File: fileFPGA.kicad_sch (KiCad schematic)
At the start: 11 parts, among them J2 UART, J6 JTAG, U3 LFE5U-25F-6BG256C, U6 W25Q128JVP

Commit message: Update Mouser prices
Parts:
- C25: Pricing (EUR) 0,11 -> 0,09
- C26: Pricing (EUR) 0,09 -> 0,02
- J2: Pricing (EUR) 0,24 -> 0,32
- J6: Pricing (EUR) 2,37 -> 3,02
- OSC1: Pricing (EUR) 1,13 -> 1,23
- R27, R30: Pricing (EUR) 0,11 -> 0,10
- U3: Pricing (EUR) 7,87 -> 14,25
- U6: Pricing (EUR) 1,52 -> 1,94
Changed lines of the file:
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@@
       (effects (font (size 1.27 1.27)) hide)
     )
-    (property "Pricing (EUR)" "2,37" (id 7) (at 218.44 27.94 0)
+    (property "Pricing (EUR)" "3,02" (id 7) (at 218.44 27.94 0)
       (effects (font (size 1.27 1.27)) hide)
     )
@@
       (effects (font (size 1.27 1.27)) hide)
     )
-    (property "Pricing (EUR)" "0,11" (id 7) (at 187.96 30.48 0)
+    (property "Pricing (EUR)" "0,10" (id 7) (at 187.96 30.48 0)
       (effects (font (size 1.27 1.27)) hide)
     )
@@
       (effects (font (size 1.27 1.27)) hide)
     )
-    (property "Pricing (EUR)" "1,52" (id 8) (at 57.15 181.61 0)
+    (property "Pricing (EUR)" "1,94" (id 8) (at 57.15 181.61 0)
       (effects (font (size 1.27 1.27)) hide)
     )
@@
       (effects (font (size 1.27 1.27)) hide)
     )
-    (property "Pricing (EUR)" "1,13" (id 7) (at 142.24 180.34 0)
+    (property "Pricing (EUR)" "1,23" (id 7) (at 142.24 180.34 0)
       (effects (font (size 1.27 1.27)) hide)
     )
@@
       (effects (font (size 1.27 1.27)) hide)
     )
-    (property "Pricing (EUR)" "0,11" (id 7) (at 179.07 66.04 0)
+    (property "Pricing (EUR)" "0,09" (id 7) (at 179.07 66.04 0)
       (effects (font (size 1.27 1.27)) hide)
     )
@@
       (effects (font (size 1.27 1.27)) hide)
     )
-    (property "Pricing (EUR)" "0,09" (id 7) (at 184.15 66.04 0)
+    (property "Pricing (EUR)" "0,02" (id 7) (at 184.15 66.04 0)
       (effects (font (size 1.27 1.27)) hide)
     )
@@
       (effects (font (size 1.27 1.27)) hide)
     )
-    (property "Pricing (EUR)" "0,11" (id 7) (at 40.64 168.91 0)
+    (property "Pricing (EUR)" "0,10" (id 7) (at 40.64 168.91 0)
       (effects (font (size 1.27 1.27)) hide)
     )
@@
       (effects (font (size 1.27 1.27)) hide)
     )
-    (property "Pricing (EUR)" "7,87" (id 7) (at 36.83 34.29 0)
+    (property "Pricing (EUR)" "14,25" (id 7) (at 36.83 34.29 0)
       (effects (font (size 1.27 1.27)) hide)
     )
@@
       (effects (font (size 1.27 1.27)) hide)
     )
-    (property "Pricing (EUR)" "7,87" (id 7) (at 121.92 31.75 0)
+    (property "Pricing (EUR)" "14,25" (id 7) (at 121.92 31.75 0)
       (effects (font (size 1.27 1.27)) hide)
     )
@@
       (effects (font (size 1.27 1.27)) hide)
     )
-    (property "Pricing (EUR)" "7,87" (id 7) (at 185.42 77.47 0)
+    (property "Pricing (EUR)" "14,25" (id 7) (at 185.42 77.47 0)
       (effects (font (size 1.27 1.27)) hide)
     )
@@
       (effects (font (size 1.27 1.27)) hide)
     )
-    (property "Pricing (EUR)" "7,87" (id 7) (at 248.92 34.29 0)
+    (property "Pricing (EUR)" "14,25" (id 7) (at 248.92 34.29 0)
       (effects (font (size 1.27 1.27)) hide)
     )
@@
       (effects (font (size 1.27 1.27)) hide)
     )
-    (property "Pricing (EUR)" "0,24" (id 7) (at 217.17 52.07 0)
-      (effects (font (size 1.27 1.27)) hide)
-    )
+    (property "Pricing (EUR)" "0,32" (id 7) (at 217.17 52.07 0)
+      (effects (font (size 1.27 1.27)) hide)
+    )

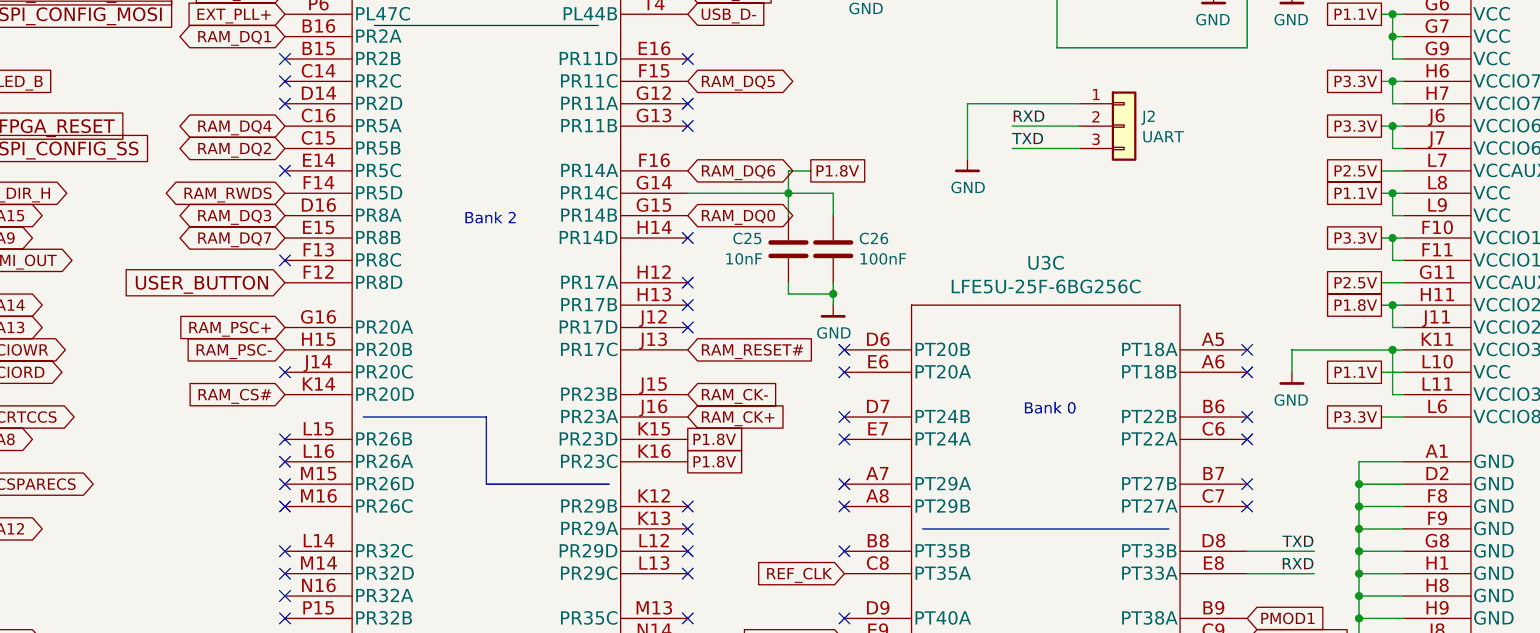
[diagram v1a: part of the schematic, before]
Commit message: Replace HyperRAM with 3V Winbond part
Also remove PSC/PSC# as they are not used on 3V parts.
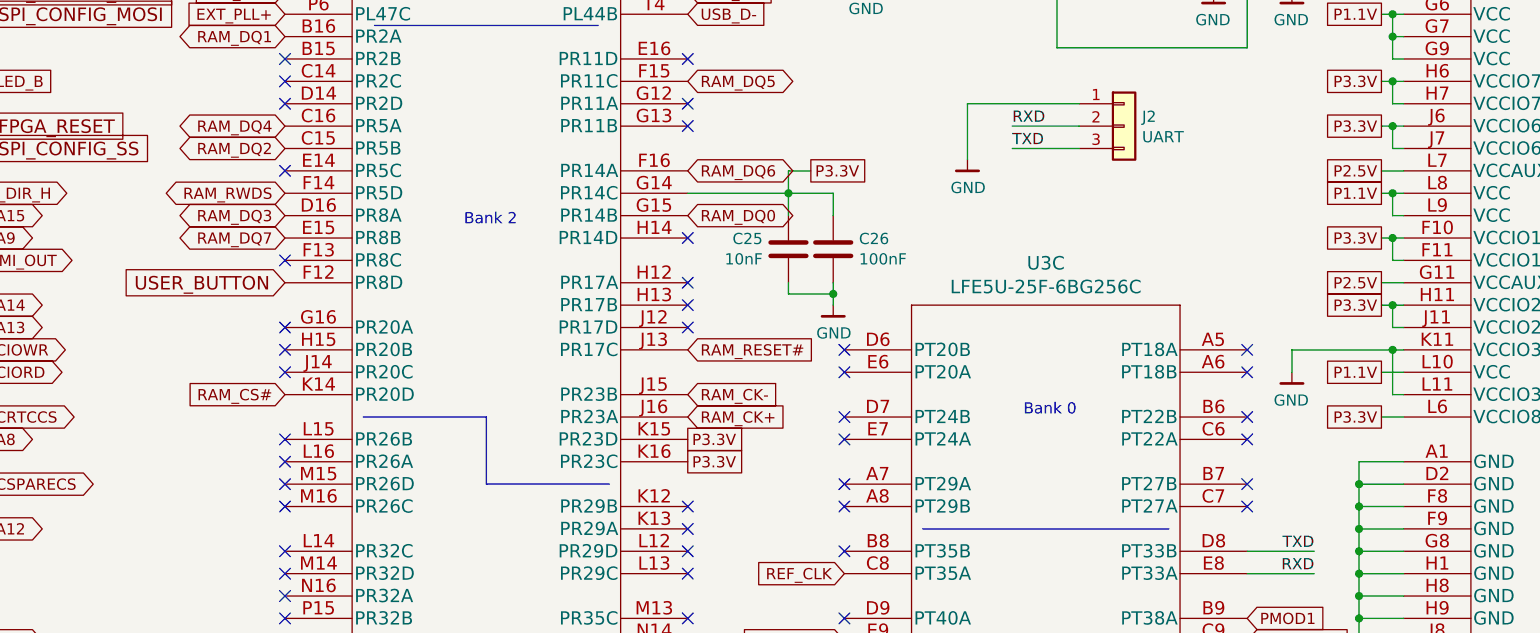
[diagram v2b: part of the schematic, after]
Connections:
- net P1.8V is gone; now on net P3.3V: C25.1, C26.1, U3.G14 (PR14C), U3.H11 (VCCIO2), U3.J11 (VCCIO2), U3.K15 (PR23D), U3.K16 (PR23C)
- net RAM_PSC+: no longer names the net of U3.G16 (PR20A)
- net RAM_PSC-: no longer names the net of U3.H15 (PR20B)
- no-connect marks 101 -> 103
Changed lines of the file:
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@@
   )
   (no_connect (at 121.92 105.41))
+  (no_connect (at 121.92 74.93))
+  (no_connect (at 121.92 77.47))
   (no_connect (at 231.14 85.09))
   (no_connect (at 87.63 135.89))
@@
     )
   )
+  (global_label "P3.3V" (shape passive) (at 167.64 87.63 0) (fields_autoplaced)
+    (effects (font (size 1.27 1.27)) (justify left))
+    (property "Intersheet References" "${INTERSHEET_REFS}" (id 0) (at 414.02 152.4 0)
+      (effects (font (size 1.27 1.27)) hide)
+    )
+  )
   (global_label "REF_CLK" (shape input) (at 152.4 181.61 0) (fields_autoplaced)
     (effects (font (size 1.27 1.27)) (justify left))
@@
     )
   )
-  (global_label "P1.8V" (shape passive) (at 181.61 57.15 0) (fields_autoplaced)
-    (effects (font (size 1.27 1.27)) (justify left))
-    (property "Intersheet References" "${INTERSHEET_REFS}" (id 0) (at 0 0 0)
-      (effects (font (size 1.27 1.27)) hide)
-    )
-  )
   (global_label "A0" (shape bidirectional) (at 121.92 31.75 180) (fields_autoplaced)
     (effects (font (size 1.27 1.27)) (justify right))
@@
     )
   )
+  (global_label "P3.3V" (shape passive) (at 181.61 57.15 0) (fields_autoplaced)
+    (effects (font (size 1.27 1.27)) (justify left))
+    (property "Intersheet References" "${INTERSHEET_REFS}" (id 0) (at 427.99 121.92 0)
+      (effects (font (size 1.27 1.27)) hide)
+    )
+  )
   (global_label "RAM_DQ7" (shape bidirectional) (at 121.92 64.77 180) (fields_autoplaced)
     (effects (font (size 1.27 1.27)) (justify right))
@@
     )
   )
-  (global_label "P1.8V" (shape passive) (at 246.38 72.39 180) (fields_autoplaced)
-    (effects (font (size 1.27 1.27)) (justify right))
-    (property "Intersheet References" "${INTERSHEET_REFS}" (id 0) (at 0 0 0)
-      (effects (font (size 1.27 1.27)) hide)
-    )
-  )
-  (global_label "RAM_PSC+" (shape input) (at 121.92 74.93 180) (fields_autoplaced)
-    (effects (font (size 1.27 1.27)) (justify right))
-    (property "Intersheet References" "${INTERSHEET_REFS}" (id 0) (at 0 0 0)
-      (effects (font (size 1.27 1.27)) hide)
-    )
-  )
   (global_label "P2.5V" (shape passive) (at 246.38 69.85 180) (fields_autoplaced)
     (effects (font (size 1.27 1.27)) (justify right))
@@
   (global_label "A6" (shape bidirectional) (at 36.83 130.81 180) (fields_autoplaced)
     (effects (font (size 1.27 1.27)) (justify right))
-    (property "Intersheet References" "${INTERSHEET_REFS}" (id 0) (at 0 0 0)
-      (effects (font (size 1.27 1.27)) hide)
-    )
-  )
-  (global_label "P1.8V" (shape passive) (at 167.64 90.17 0) (fields_autoplaced)
-    (effects (font (size 1.27 1.27)) (justify left))
     (property "Intersheet References" "${INTERSHEET_REFS}" (id 0) (at 0 0 0)
       (effects (font (size 1.27 1.27)) hide)
@@
     )
   )
-  (global_label "RAM_PSC-" (shape input) (at 121.92 77.47 180) (fields_autoplaced)
-    (effects (font (size 1.27 1.27)) (justify right))
-    (property "Intersheet References" "${INTERSHEET_REFS}" (id 0) (at 0 0 0)
-      (effects (font (size 1.27 1.27)) hide)
-    )
-  )
   (global_label "A10" (shape bidirectional) (at 87.63 110.49 0) (fields_autoplaced)
     (effects (font (size 1.27 1.27)) (justify left))
@@
     )
   )
+  (global_label "P3.3V" (shape passive) (at 246.38 72.39 180) (fields_autoplaced)
+    (effects (font (size 1.27 1.27)) (justify right))
+    (property "Intersheet References" "${INTERSHEET_REFS}" (id 0) (at 0 7.62 0)
+      (effects (font (size 1.27 1.27)) hide)
+    )
+  )
   (global_label "A_~{EN}_L" (shape output) (at 36.83 115.57 180) (fields_autoplaced)
     (effects (font (size 1.27 1.27)) (justify right))
@@
   )
   (global_label "A11" (shape bidirectional) (at 87.63 113.03 0) (fields_autoplaced)
-    (effects (font (size 1.27 1.27)) (justify left))
-    (property "Intersheet References" "${INTERSHEET_REFS}" (id 0) (at 0 0 0)
-      (effects (font (size 1.27 1.27)) hide)
-    )
-  )
-  (global_label "P1.8V" (shape passive) (at 167.64 87.63 0) (fields_autoplaced)
     (effects (font (size 1.27 1.27)) (justify left))
     (property "Intersheet References" "${INTERSHEET_REFS}" (id 0) (at 0 0 0)
@@
       (effects (font (size 1.27 1.27)) hide)
     )
+  )
+  (global_label "P3.3V" (shape passive) (at 167.64 90.17 0) (fields_autoplaced)
+    (effects (font (size 1.27 1.27)) (justify left))
+    (property "Intersheet References" "${INTERSHEET_REFS}" (id 0) (at 414.02 154.94 0)
+      (effects (font (size 1.27 1.27)) hide)
+    )

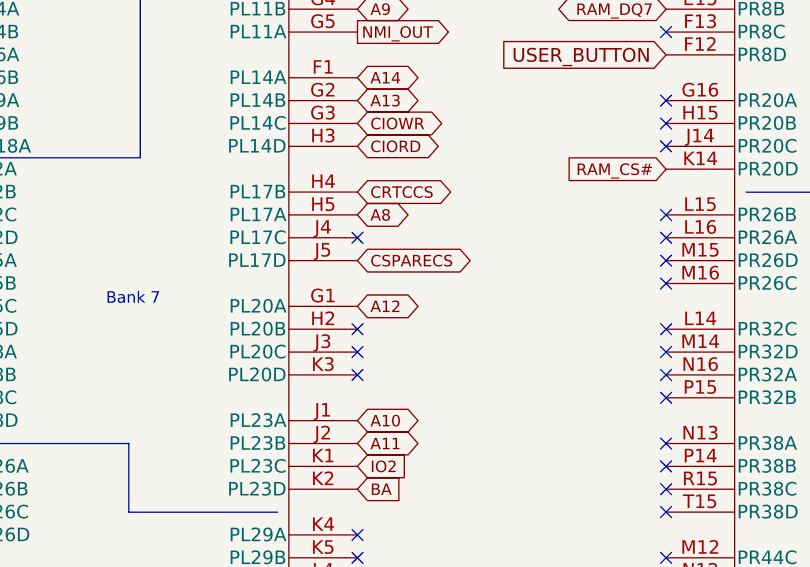
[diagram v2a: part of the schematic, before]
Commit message: Add NMI and IRQ inputs
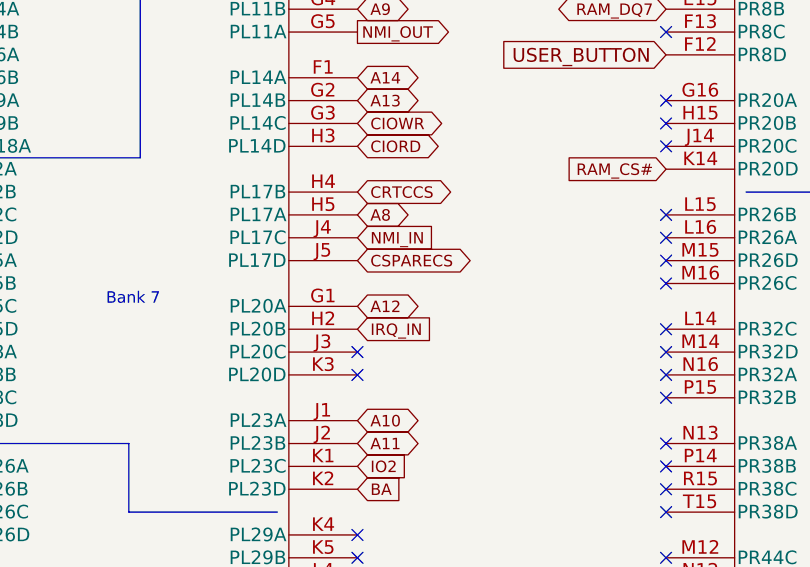
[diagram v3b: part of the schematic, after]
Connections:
- net IRQ_IN: now reaches U3.H2 (PL20B)
- net NMI_IN: now reaches U3.J4 (PL17C)
- no-connect marks 103 -> 101
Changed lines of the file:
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@@
   (no_connect (at 167.64 138.43))
   (no_connect (at 231.14 77.47))
-  (no_connect (at 87.63 90.17))
   (no_connect (at 167.64 95.25))
   (no_connect (at 167.64 156.21))
   (no_connect (at 36.83 72.39))
   (no_connect (at 121.92 49.53))
-  (no_connect (at 87.63 100.33))
   (no_connect (at 121.92 80.01))
   (no_connect (at 167.64 148.59))
@@
     )
   )
+  (global_label "IRQ_IN" (shape input) (at 87.63 100.33 0) (fields_autoplaced)
+    (effects (font (size 1.27 1.27)) (justify left))
+    (property "Intersheet References" "${INTERSHEET_REFS}" (id 0) (at 96.0623 100.2506 0)
+      (effects (font (size 1.27 1.27)) (justify left) hide)
+    )
+  )
   (global_label "A8" (shape bidirectional) (at 87.63 87.63 0) (fields_autoplaced)
     (effects (font (size 1.27 1.27)) (justify left))
@@
     )
   )
+  (global_label "NMI_IN" (shape input) (at 87.63 90.17 0) (fields_autoplaced)
+    (effects (font (size 1.27 1.27)) (justify left))
+    (property "Intersheet References" "${INTERSHEET_REFS}" (id 0) (at 96.2437 90.0906 0)
+      (effects (font (size 1.27 1.27)) (justify left) hide)
+    )
+  )

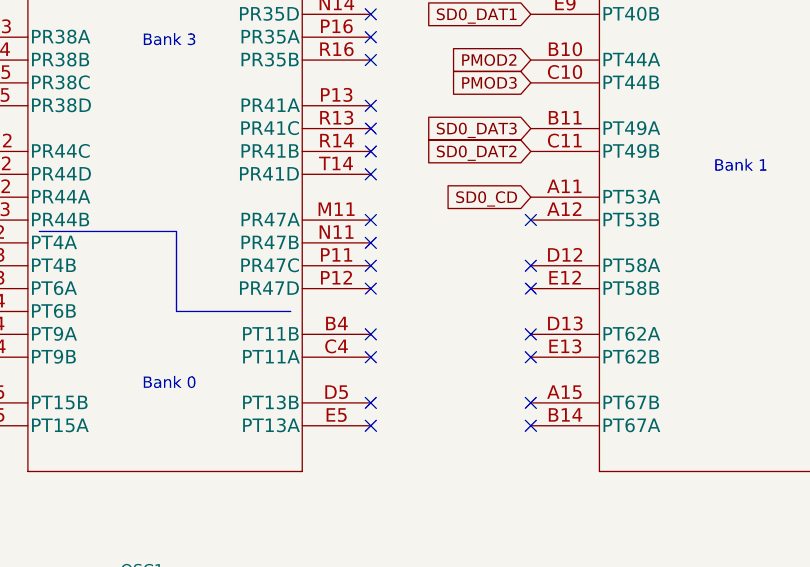
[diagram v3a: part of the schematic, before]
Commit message: Redo routing to memories
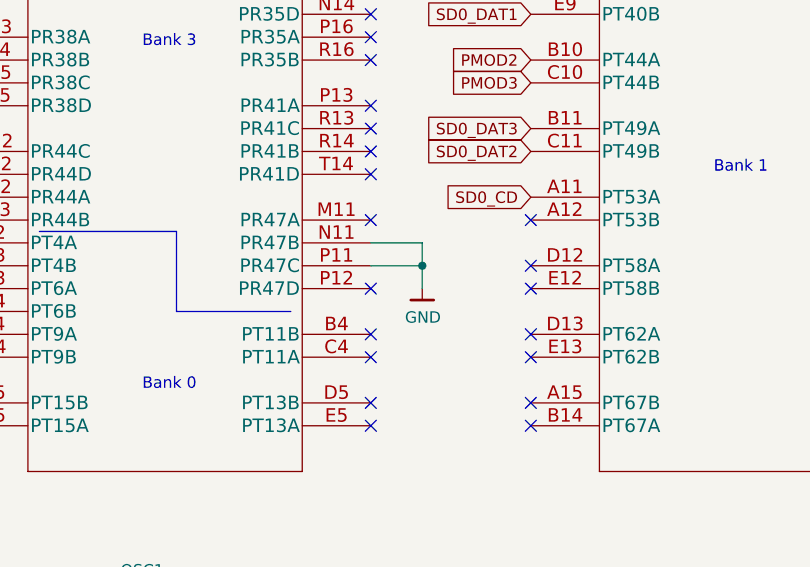
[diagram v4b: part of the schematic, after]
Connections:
- net GND: now also U3.N11 (PR47B), U3.P11 (PR47C)
- no-connect marks 101 -> 99
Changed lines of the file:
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@@
   (junction (at 243.84 156.21) (diameter 0) (color 0 0 0 0)
   )
+  (junction (at 173.355 138.43) (diameter 0) (color 0 0 0 0)
+  )
   (junction (at 184.15 71.12) (diameter 0) (color 0 0 0 0)
   )
@@
   (no_connect (at 185.42 92.71))
   (no_connect (at 231.14 80.01))
-  (no_connect (at 167.64 135.89))
   (no_connect (at 121.92 125.73))
   (no_connect (at 185.42 100.33))
@@
   (no_connect (at 231.14 92.71))
   (no_connect (at 231.14 148.59))
-  (no_connect (at 167.64 138.43))
   (no_connect (at 231.14 77.47))
   (no_connect (at 167.64 95.25))
@@
     (stroke (width 0) (type default) (color 0 0 0 0))
   )
+  (wire (pts (xy 173.355 135.89) (xy 173.355 138.43))
+    (stroke (width 0) (type default) (color 0 0 0 0))
+  )
   (wire (pts (xy 246.38 57.15) (xy 248.92 57.15))
     (stroke (width 0) (type default) (color 0 0 0 0))
@@
     (stroke (width 0) (type default) (color 0 0 0 0))
   )
+  (wire (pts (xy 173.355 138.43) (xy 173.355 140.97))
+    (stroke (width 0) (type default) (color 0 0 0 0))
+  )
   (wire (pts (xy 243.84 90.17) (xy 243.84 92.71))
     (stroke (width 0) (type default) (color 0 0 0 0))
@@
     (stroke (width 0) (type default) (color 0 0 0 0))
   )
+  (wire (pts (xy 167.64 138.43) (xy 173.355 138.43))
+    (stroke (width 0) (type default) (color 0 0 0 0))
+  )
   (wire (pts (xy 246.38 64.77) (xy 247.65 64.77))
     (stroke (width 0) (type default) (color 0 0 0 0))
@@
     (stroke (width 0) (type default) (color 0 0 0 0))
   )
+  (wire (pts (xy 167.64 135.89) (xy 173.355 135.89))
+    (stroke (width 0) (type default) (color 0 0 0 0))
+  )
   (wire (pts (xy 231.14 100.33) (xy 238.76 100.33))
     (stroke (width 0) (type default) (color 0 0 0 0))
@@
     (pin "2")
   )
+  (symbol (lib_id "gkl_power:GND") (at 173.355 140.97 0) (unit 1)
+    (in_bom yes) (on_board yes)
+    (property "Reference" "#PWR?" (id 0) (at 173.355 147.32 0)
+      (effects (font (size 1.27 1.27)) hide)
+    )
+    (property "Value" "GND" (id 1) (at 173.4312 144.1704 0))
+    (property "Footprint" "" (id 2) (at 170.815 149.86 0)
+      (effects (font (size 1.27 1.27)) hide)
+    )
+    (property "Datasheet" "" (id 3) (at 173.355 140.97 0)
+      (effects (font (size 1.27 1.27)) hide)
+    )
+    (pin "1")
+  )
 )
